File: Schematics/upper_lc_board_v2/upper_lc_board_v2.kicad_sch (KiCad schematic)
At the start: 0 parts

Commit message: review work
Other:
- note added: "- added pwr switching for PTs - removed TCs"
- note removed: "- added pwr switching for solenoids and PTs - removed TCs"
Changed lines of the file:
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@@
 		(comment 2 "Jeevan Sanchez")
 	)
-	(text "- added pwr switching for solenoids and PTs\n- removed TCs "
+	(text "- added pwr switching for PTs\n- removed TCs "
 		(exclude_from_sim no)
 		(at 218.186 55.626 0)

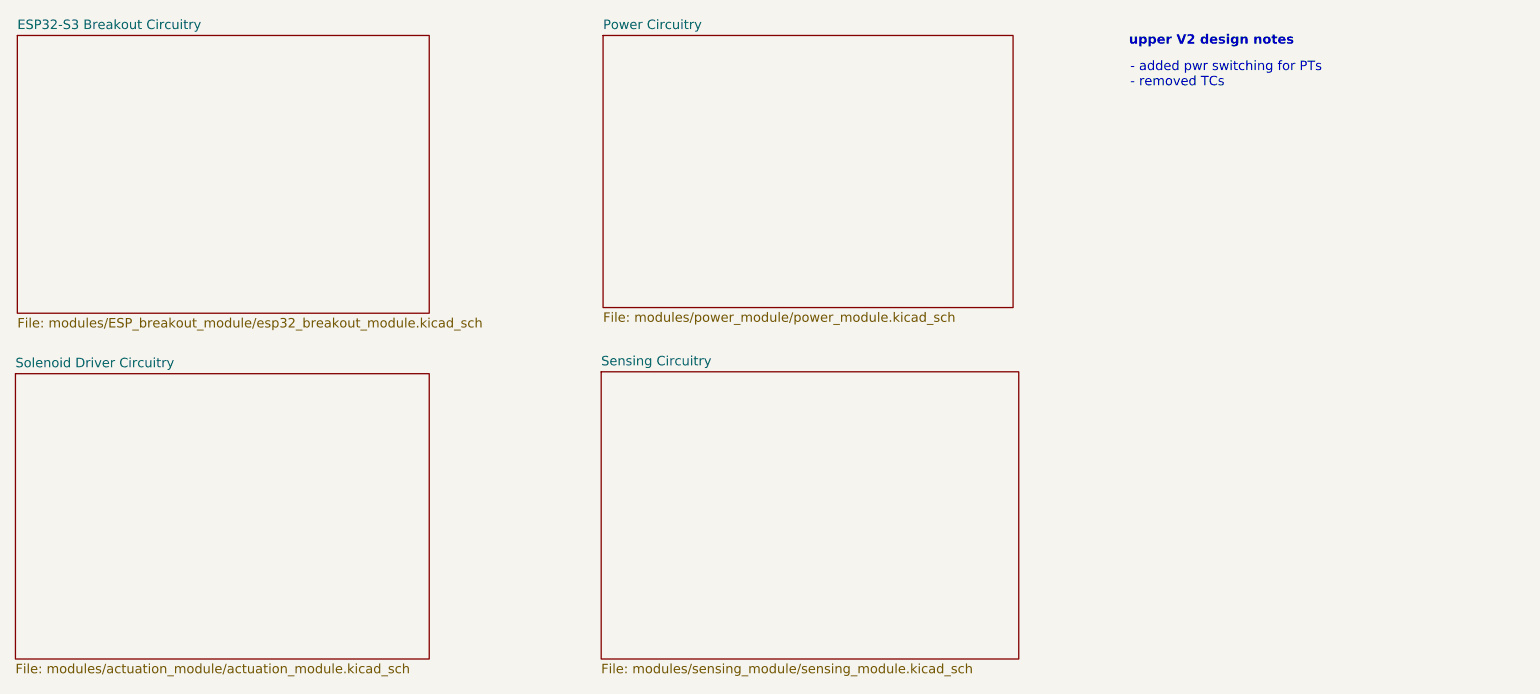
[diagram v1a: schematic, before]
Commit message: layout updates after review, cleaned up schematic organization
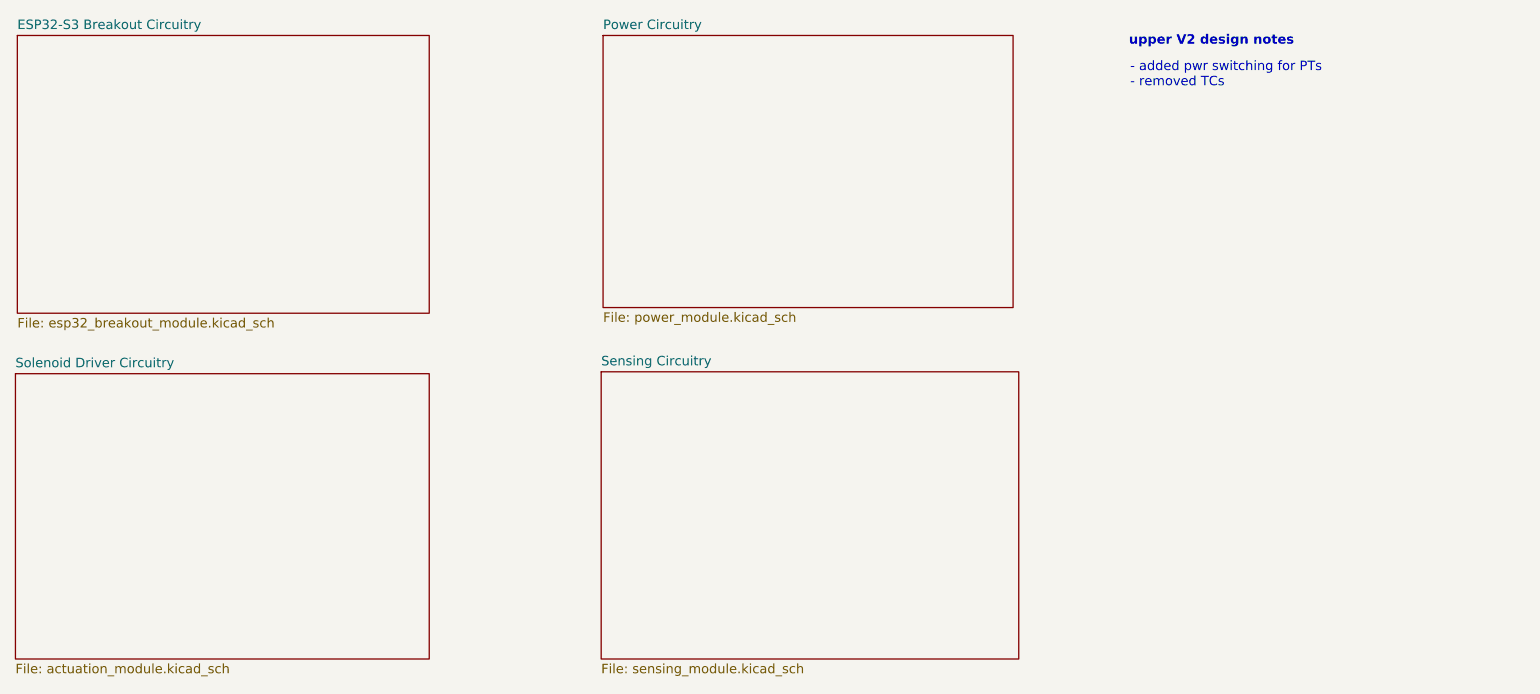
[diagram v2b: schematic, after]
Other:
- sheet ESP32-S3 Breakout Circuitry: file modules/ESP_breakout_module/esp32_breakout_module.kicad_sch -> esp32_breakout_module.kicad_sch
- sheet Power Circuitry: file modules/power_module/power_module.kicad_sch -> power_module.kicad_sch
- sheet Sensing Circuitry: file modules/sensing_module/sensing_module.kicad_sch -> sensing_module.kicad_sch
- sheet Solenoid Driver Circuitry: file modules/actuation_module/actuation_module.kicad_sch -> actuation_module.kicad_sch
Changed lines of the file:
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@@
 			)
 		)
-		(property "Sheetfile" "modules/sensing_module/sensing_module.kicad_sch"
+		(property "Sheetfile" "sensing_module.kicad_sch"
 			(at 147.066 134.6966 0)
 			(effects
@@
 			)
 		)
-		(property "Sheetfile" "modules/power_module/power_module.kicad_sch"
+		(property "Sheetfile" "power_module.kicad_sch"
 			(at 147.32 87.4526 0)
 			(effects
@@
 			)
 		)
-		(property "Sheetfile" "modules/actuation_module/actuation_module.kicad_sch"
+		(property "Sheetfile" "actuation_module.kicad_sch"
 			(at 68.326 134.6966 0)
 			(effects
@@
 			)
 		)
-		(property "Sheetfile" "modules/ESP_breakout_module/esp32_breakout_module.kicad_sch"
+		(property "Sheetfile" "esp32_breakout_module.kicad_sch"
 			(at 68.58 88.2146 0)
 			(effects
